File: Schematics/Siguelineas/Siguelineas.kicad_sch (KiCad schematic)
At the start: 25 parts, among them J1 Batt_Input, J11 SD_con, J2 FAN_IN, J3 Line_Sensors, J3 TB6612FNG_A, J4 IMU, J4 TB6612FNG_B, J5 SCREEN, J8 Motor_1, J9 Motor_2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

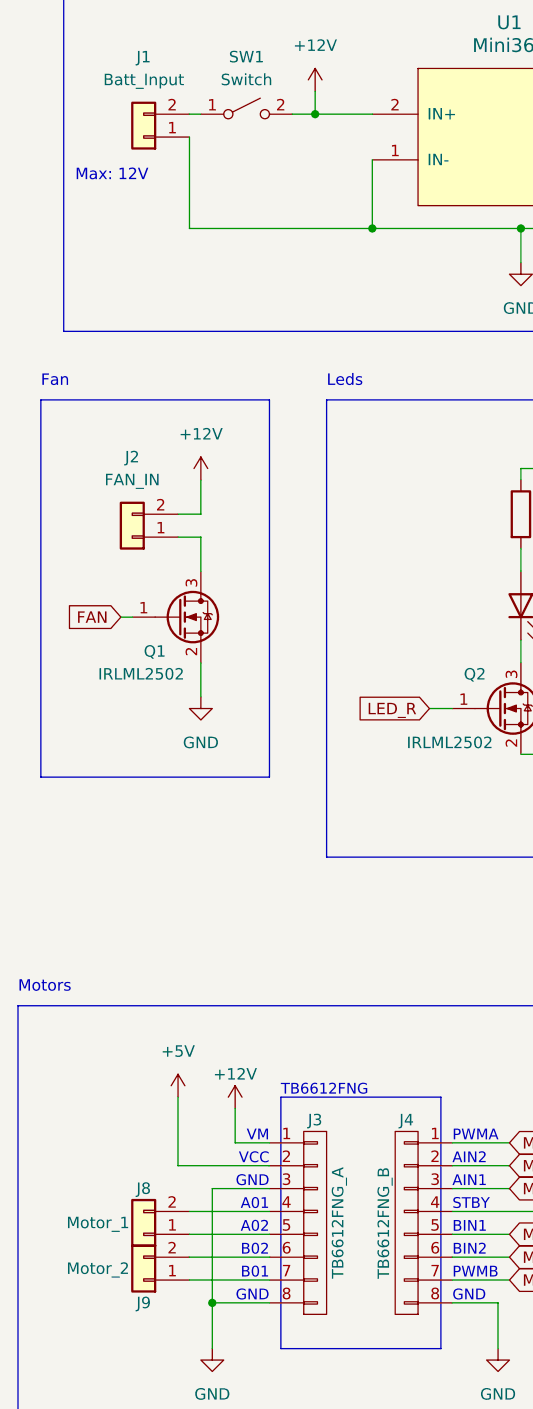
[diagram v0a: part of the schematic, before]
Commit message: Changed motor conectors position
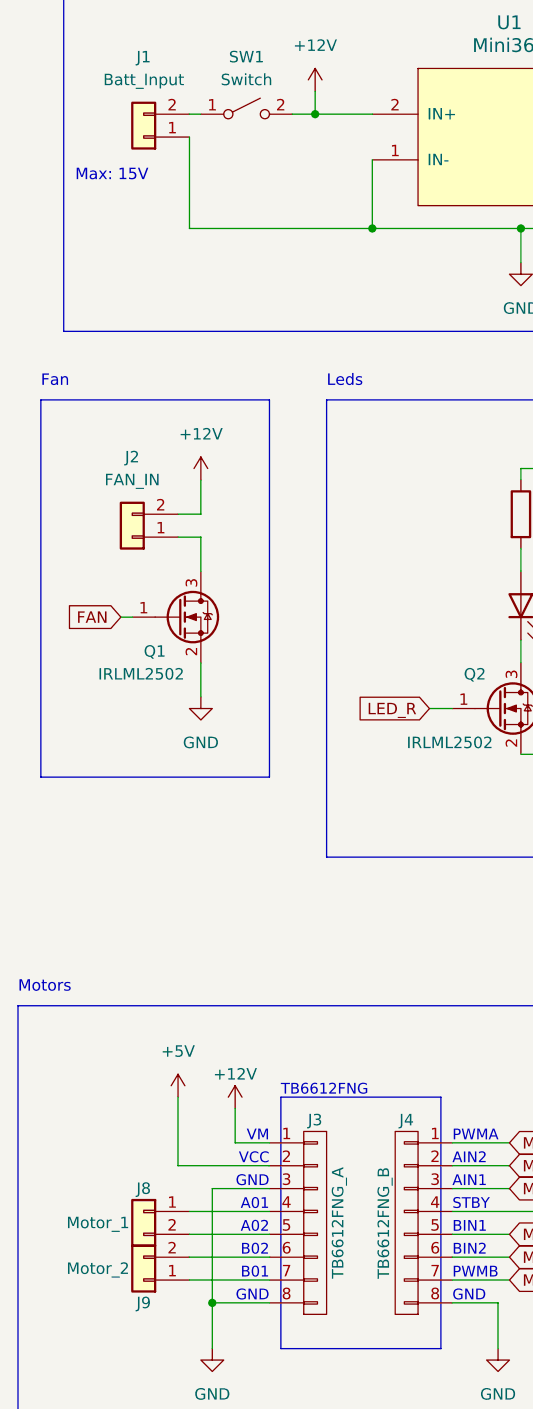
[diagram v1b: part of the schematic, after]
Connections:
- net at J3.4 (P4): now also J8.1 (Pin_1); no longer J8.2 (Pin_2)
- net at J3.5 (P5): now also J8.2 (Pin_2); no longer J8.1 (Pin_1)
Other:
- note added: "Max: 15V"
- note removed: "Max: 12V"
- moved on the sheet: J8
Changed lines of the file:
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@@
+    (stroke (width 0) (type default))
+  )
+  (wire (pts (xy 40.64 161.29) (xy 49.53 161.29))
     (stroke (width 0) (type default))
   )
@@
     (stroke (width 0) (type default))
   )
+  (wire (pts (xy 40.64 158.75) (xy 49.53 158.75))
+    (stroke (width 0) (type default))
+  )
   (wire (pts (xy 175.26 93.98) (xy 177.8 93.98))
     (stroke (width 0) (type default))
@@
     (stroke (width 0) (type default))
   )
-  (wire (pts (xy 40.64 158.75) (xy 49.53 158.75))
-    (stroke (width 0) (type default))
-  )
   (wire (pts (xy 76.2 151.13) (xy 69.85 151.13))
     (stroke (width 0) (type default))
@@
   )
   (wire (pts (xy 175.26 66.04) (xy 177.8 66.04))
-    (stroke (width 0) (type default))
-  )
-  (wire (pts (xy 40.64 161.29) (xy 49.53 161.29))
     (stroke (width 0) (type default))
   )
@@
     (effects (font (size 1.1938 1.1938)) (justify right bottom))
   )
-  (text "Max: 12V" (at 27.94 44.45 0)
+  (text "Max: 15V" (at 27.94 44.45 0)
     (effects (font (size 1.27 1.27)) (justify left bottom))
   )
@@
     )
   )
-  (symbol (lib_id "Connector_Generic:Conn_01x02") (at 35.56 161.29 180) (unit 1)
+  (symbol (lib_id "Connector_Generic:Conn_01x02") (at 35.56 158.75 0) (mirror y) (unit 1)
     (in_bom yes) (on_board yes) (dnp no)
     (property "Reference" "J8" (at 35.56 156.21 0)
@@
       (effects (font (size 1.27 1.27)))
     )
-    (property "Footprint" "Connector_JST:JST_PH_B2B-PH-K_1x02_P2.00mm_Vertical" (at 35.56 161.29 0)
-      (effects (font (size 1.27 1.27)) hide)
-    )
-    (property "Datasheet" "~" (at 35.56 161.29 0)
-      (effects (font (size 1.27 1.27)) hide)
-    )
+    (property "Footprint" "Connector_JST:JST_PH_B2B-PH-K_1x02_P2.00mm_Vertical" (at 35.56 158.75 0)
+      (effects (font (size 1.27 1.27)) hide)
+    )
+    (property "Datasheet" "~" (at 35.56 158.75 0)
+      (effects (font (size 1.27 1.27)) hide)
+    )

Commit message: Version 1.0
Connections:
- net +12V: now also J1.2 (Pin_2); no longer SW1.2 (B)
- net +5V: now also SW1.2 (B); no longer U1.4 (OUT+)
- net at SW1.1 (A): now also U1.4 (OUT+); no longer J1.2 (Pin_2)
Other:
- moved on the sheet: SW1, U1
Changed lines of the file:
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@@
     (comment 1 "Adrian Martinez")
   )
+  (junction (at 44.45 36.83) (diameter 0) (color 0 0 0 0)
+  )
   (junction (at 82.55 107.95) (diameter 0) (color 0 0 0 0)
   )
-  (junction (at 54.61 36.83) (diameter 0) (color 0 0 0 0)
-  )
   (junction (at 256.54 138.43) (diameter 0) (color 0 0 0 0)
   )
@@
   (junction (at 143.51 139.7) (diameter 0) (color 0 0 0 0)
   )
-  (junction (at 60.96 49.53) (diameter 0) (color 0 0 0 0)
+  (junction (at 63.5 49.53) (diameter 0) (color 0 0 0 0)
   )
   (junction (at 259.08 125.73) (diameter 0) (color 0 0 0 0)
@@
   (junction (at 256.54 148.59) (diameter 0) (color 0 0 0 0)
   )
-  (junction (at 77.47 49.53) (diameter 0) (color 0 0 0 0)
-  )
   (junction (at 256.54 140.97) (diameter 0) (color 0 0 0 0)
   )
   (junction (at 43.18 168.91) (diameter 0) (color 0 0 0 0)
+  )
+  (junction (at 48.26 49.53) (diameter 0) (color 0 0 0 0)
   )
   (junction (at 143.51 163.83) (diameter 0) (color 0 0 0 0)
@@
   (no_connect (at 262.89 143.51))
   (no_connect (at 262.89 146.05))
-  (wire (pts (xy 52.07 36.83) (xy 54.61 36.83))
-    (stroke (width 0) (type default))
-  )
   (wire (pts (xy 40.64 161.29) (xy 49.53 161.29))
     (stroke (width 0) (type default))
@@
     (stroke (width 0) (type default))
   )
+  (wire (pts (xy 63.5 49.53) (xy 78.74 49.53))
+    (stroke (width 0) (type default))
+  )
   (wire (pts (xy 40.64 158.75) (xy 49.53 158.75))
     (stroke (width 0) (type default))
@@
     (stroke (width 0) (type default))
   )
-  (wire (pts (xy 54.61 36.83) (xy 54.61 34.29))
+  (wire (pts (xy 44.45 36.83) (xy 44.45 34.29))
     (stroke (width 0) (type default))
   )
@@
     (stroke (width 0) (type default))
   )
+  (wire (pts (xy 44.45 36.83) (xy 48.26 36.83))
+    (stroke (width 0) (type default))
+  )
   (wire (pts (xy 87.63 95.25) (xy 87.63 97.79))
     (stroke (width 0) (type default))
@@
     (stroke (width 0) (type default))
   )
-  (wire (pts (xy 60.96 41.91) (xy 60.96 49.53))
+  (wire (pts (xy 48.26 41.91) (xy 48.26 49.53))
     (stroke (width 0) (type default))
   )
@@
     (stroke (width 0) (type default))
   )
+  (wire (pts (xy 91.44 36.83) (xy 95.25 36.83))
+    (stroke (width 0) (type default))
+  )
   (wire (pts (xy 256.54 138.43) (xy 262.89 138.43))
     (stroke (width 0) (type default))
@@
     (stroke (width 0) (type default))
   )
+  (wire (pts (xy 48.26 49.53) (xy 63.5 49.53))
+    (stroke (width 0) (type default))
+  )
   (wire (pts (xy 237.49 39.37) (xy 228.6 39.37))
     (stroke (width 0) (type default))
@@
     (stroke (width 0) (type default))
   )
-  (wire (pts (xy 91.44 36.83) (xy 95.25 36.83))
-    (stroke (width 0) (type default))
-  )
   (wire (pts (xy 39.37 83.82) (xy 41.91 83.82))
     (stroke (width 0) (type default))
@@
     (stroke (width 0) (type default))
   )
+  (wire (pts (xy 78.74 36.83) (xy 81.28 36.83))
+    (stroke (width 0) (type default))
+  )
   (wire (pts (xy 41.91 77.47) (xy 41.91 81.28))
     (stroke (width 0) (type default))
@@
     (stroke (width 0) (type default))
   )
-  (wire (pts (xy 77.47 49.53) (xy 77.47 53.34))
+  (wire (pts (xy 63.5 49.53) (xy 63.5 52.07))
     (stroke (width 0) (type default))
   )
@@
     (stroke (width 0) (type default))
   )
-  (wire (pts (xy 54.61 36.83) (xy 60.96 36.83))
-    (stroke (width 0) (type default))
-  )
-  (wire (pts (xy 40.64 49.53) (xy 60.96 49.53))
+  (wire (pts (xy 40.64 49.53) (xy 48.26 49.53))
     (stroke (width 0) (type default))
   )
@@
     (stroke (width 0) (type default))
   )
-  (wire (pts (xy 40.64 36.83) (xy 41.91 36.83))
-    (stroke (width 0) (type default))
-  )
   (wire (pts (xy 76.2 153.67) (xy 69.85 153.67))
     (stroke (width 0) (type default))
@@
     (stroke (width 0) (type default))
   )
-  (wire (pts (xy 60.96 49.53) (xy 77.47 49.53))
-    (stroke (width 0) (type default))
-  )
   (wire (pts (xy 175.26 101.6) (xy 176.53 101.6))
     (stroke (width 0) (type default))
@@
     (stroke (width 0) (type default))
   )
-  (wire (pts (xy 91.44 49.53) (xy 77.47 49.53))
-    (stroke (width 0) (type default))
-  )
   (wire (pts (xy 49.53 166.37) (xy 40.64 166.37))
     (stroke (width 0) (type default))
   )
+  (wire (pts (xy 40.64 36.83) (xy 44.45 36.83))
+    (stroke (width 0) (type default))
+  )
   (wire (pts (xy 82.55 76.2) (xy 87.63 76.2))
     (stroke (width 0) (type default))
@@
     (stroke (width 0) (type default))
   )
-  (wire (pts (xy 91.44 41.91) (xy 91.44 49.53))
+  (wire (pts (xy 78.74 41.91) (xy 78.74 49.53))
     (stroke (width 0) (type default))
   )
@@
     )
   )
-  (symbol (lib_id "Switch:SW_SPST") (at 46.99 36.83 0) (unit 1)
-    (in_bom yes) (on_board yes) (dnp no) (fields_autoplaced)
-    (property "Reference" "SW1" (at 46.99 30.48 0)
-      (effects (font (size 1.27 1.27)))
-    )
-    (property "Value" "Switch" (at 46.99 33.02 0)
-      (effects (font (size 1.27 1.27)))
-    )
-    (property "Footprint" "Button_Switch_THT:SW_CuK_OS102011MA1QN1_SPDT_Angled" (at 46.99 36.83 0)
-      (effects (font (size 1.27 1.27)) hide)
-    )
-    (property "Datasheet" "~" (at 46.99 36.83 0)
+  (symbol (lib_id "Switch:SW_SPST") (at 86.36 36.83 0) (unit 1)
+    (in_bom yes) (on_board yes) (dnp no) (fields_autoplaced)
+    (property "Reference" "SW1" (at 86.36 30.48 0)
+      (effects (font (size 1.27 1.27)))
+    )
+    (property "Value" "Switch" (at 86.36 33.02 0)
+      (effects (font (size 1.27 1.27)))
+    )
+    (property "Footprint" "Button_Switch_THT:SW_CuK_OS102011MA1QN1_SPDT_Angled" (at 86.36 36.83 0)
+      (effects (font (size 1.27 1.27)) hide)
+    )
+    (property "Datasheet" "~" (at 86.36 36.83 0)
       (effects (font (size 1.27 1.27)) hide)
     )
@@
     )
   )
-  (symbol (lib_id "power:+12V") (at 54.61 34.29 0) (unit 1)
-    (in_bom yes) (on_board yes) (dnp no) (fields_autoplaced)
-    (property "Reference" "#PWR01" (at 54.61 38.1 0)
-      (effects (font (size 1.27 1.27)) hide)
-    )
-    (property "Value" "+12V" (at 54.61 29.21 0)
-      (effects (font (size 1.27 1.27)))
-    )
-    (property "Footprint" "" (at 54.61 34.29 0)
-      (effects (font (size 1.27 1.27)) hide)
-    )
-    (property "Datasheet" "" (at 54.61 34.29 0)
+  (symbol (lib_id "power:+12V") (at 44.45 34.29 0) (unit 1)
+    (in_bom yes) (on_board yes) (dnp no) (fields_autoplaced)
+    (property "Reference" "#PWR01" (at 44.45 38.1 0)
+      (effects (font (size 1.27 1.27)) hide)
+    )
+    (property "Value" "+12V" (at 44.45 29.21 0)
+      (effects (font (size 1.27 1.27)))
+    )
+    (property "Footprint" "" (at 44.45 34.29 0)
+      (effects (font (size 1.27 1.27)) hide)
+    )
+    (property "Datasheet" "" (at 44.45 34.29 0)
       (effects (font (size 1.27 1.27)) hide)
     )
@@
     )
   )
-  (symbol (lib_id "power:GND") (at 77.47 53.34 0) (unit 1)
+  (symbol (lib_id "power:GND") (at 63.5 52.07 0) (unit 1)
     (in_bom yes) (on_board yes) (dnp no)
-    (property "Reference" "#PWR02" (at 77.47 59.69 0)
-      (effects (font (size 1.27 1.27)) hide)
-    )
-    (property "Value" "GND" (at 77.47 58.42 0)
-      (effects (font (size 1.27 1.27)))
-    )
-    (property "Footprint" "" (at 77.47 53.34 0)
-      (effects (font (size 1.27 1.27)) hide)
-    )
-    (property "Datasheet" "" (at 77.47 53.34 0)
+    (property "Reference" "#PWR02" (at 63.5 58.42 0)
+      (effects (font (size 1.27 1.27)) hide)
+    )
+    (property "Value" "GND" (at 63.5 57.15 0)
+      (effects (font (size 1.27 1.27)))
+    )
+    (property "Footprint" "" (at 63.5 52.07 0)
+      (effects (font (size 1.27 1.27)) hide)
+    )
+    (property "Datasheet" "" (at 63.5 52.07 0)
       (effects (font (size 1.27 1.27)) hide)
     )
@@
     )
   )
-  (symbol (lib_id "mini360:Mini360") (at 76.2 39.37 0) (unit 1)
-    (in_bom yes) (on_board yes) (dnp no) (fields_autoplaced)
-    (property "Reference" "U1" (at 76.2 26.67 0)
+  (symbol (lib_id "mini360:Mini360") (at 63.5 39.37 0) (unit 1)
+    (in_bom yes) (on_board yes) (dnp no) (fields_autoplaced)
+    (property "Reference" "U1" (at 63.5 26.67 0)
       (effects (font (size 1.524 1.524)))
     )
-    (property "Value" "Mini360" (at 76.2 29.21 0)
+    (property "Value" "Mini360" (at 63.5 29.21 0)
       (effects (font (size 1.524 1.524)))
     )
-    (property "Footprint" "Mini360_step-down:Mini360_step-down" (at 76.2 39.37 0)
+    (property "Footprint" "Mini360_step-down:Mini360_step-down" (at 63.5 39.37 0)
       (effects (font (size 1.524 1.524)) hide)
     )
-    (property "Datasheet" "" (at 76.2 39.37 0)
+    (property "Datasheet" "" (at 63.5 39.37 0)
       (effects (font (size 1.524 1.524)) hide)
     )

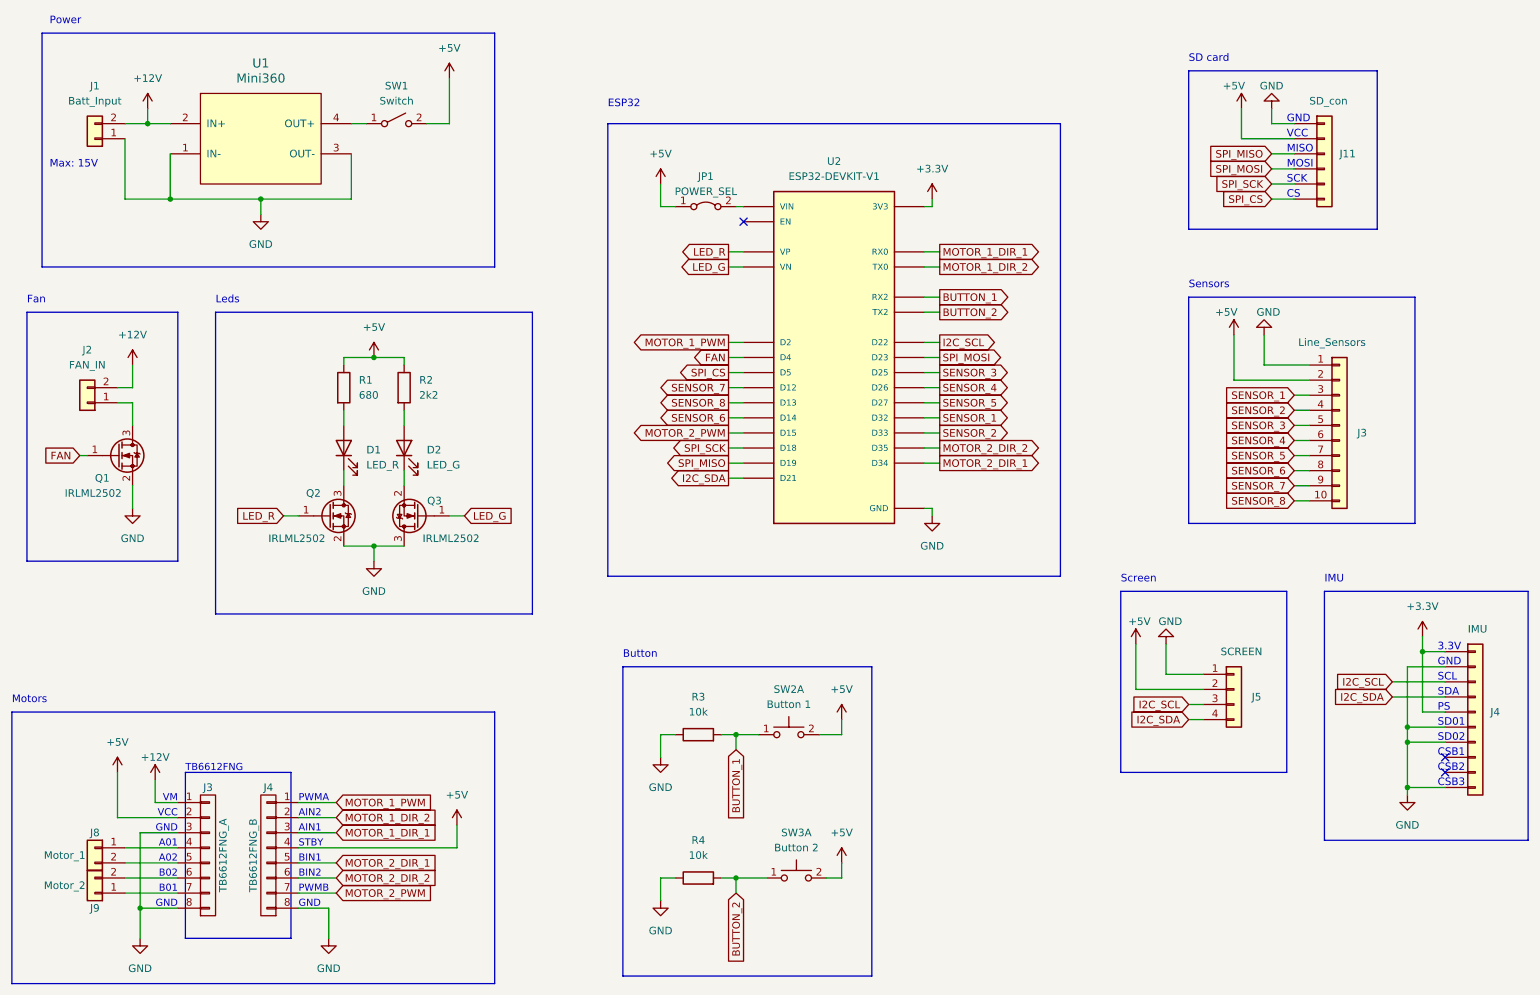
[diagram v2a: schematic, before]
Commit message: Big clean to remove unused componentes, board reworked, v1.1
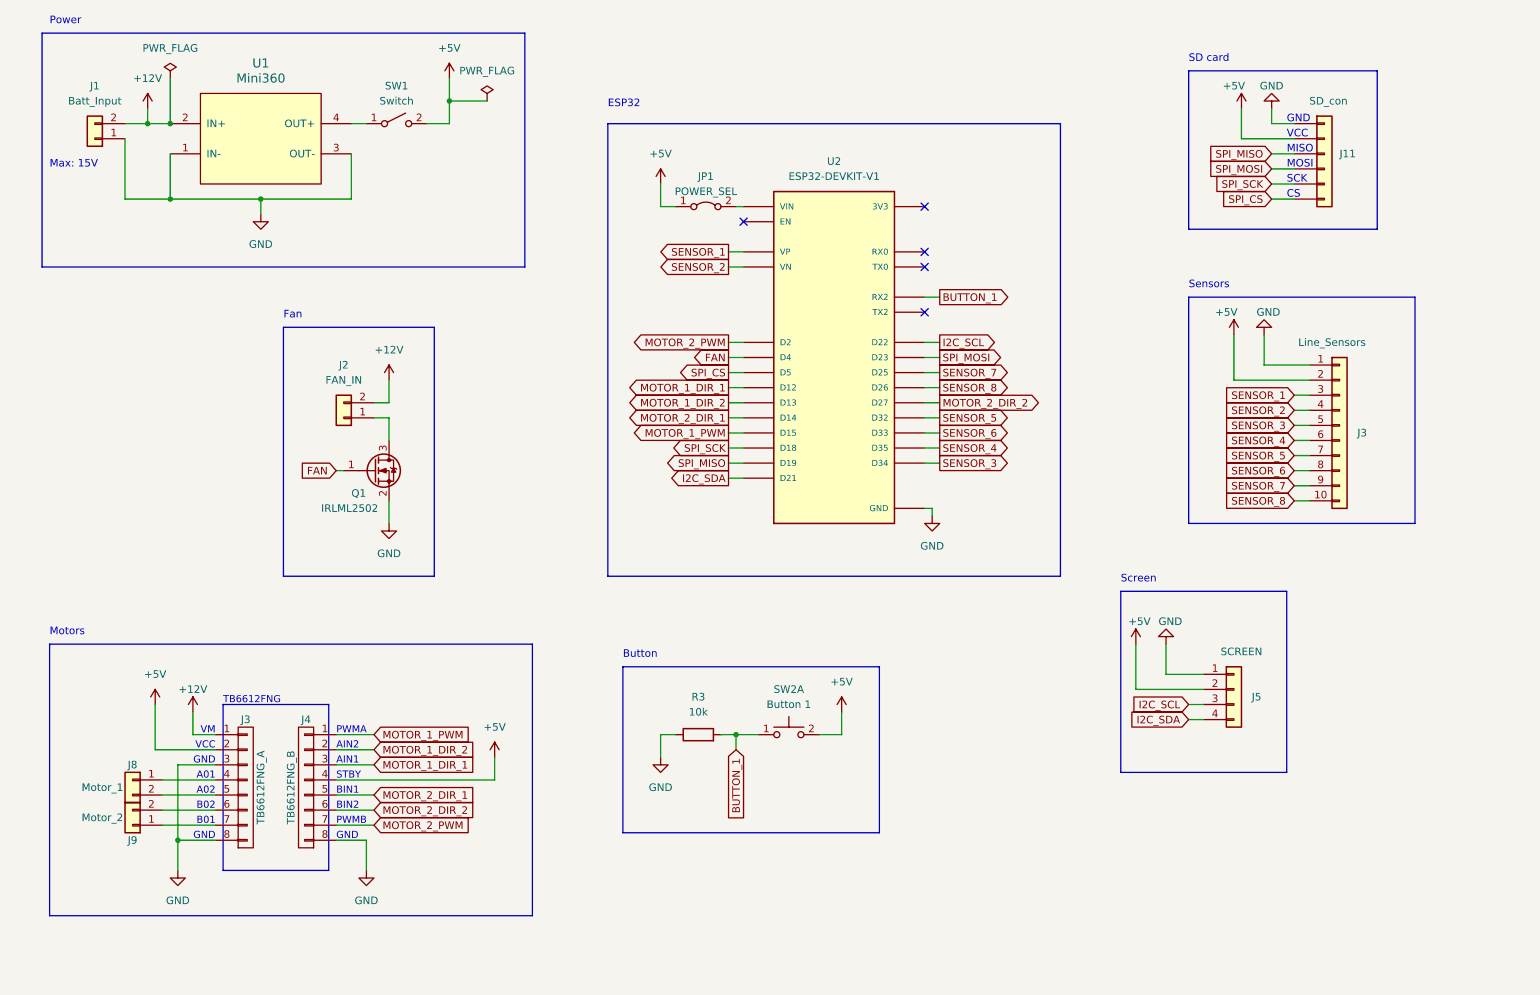
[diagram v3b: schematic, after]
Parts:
- removed D1: LED_R, Diode_SMD:D_1206_3216Metric_Pad1.42x1.75mm_HandSolder, symbol Device:LED
- removed D2: LED_G, Diode_SMD:D_1206_3216Metric_Pad1.42x1.75mm_HandSolder, symbol Device:LED
- removed J4: IMU, Connector_PinSocket_2.54mm:PinSocket_1x10_P2.54mm_Vertical, symbol Connector_Generic:Conn_01x10
- removed Q2, Q3: IRLML2502, Package_TO_SOT_SMD:SOT-23, symbol Device:Q_NMOS_GSD
- removed R1: 680, Resistor_SMD:R_1206_3216Metric_Pad1.30x1.75mm_HandSolder, symbol Device:R
- removed R2: 2k2, Resistor_SMD:R_1206_3216Metric_Pad1.30x1.75mm_HandSolder, symbol Device:R
- removed R4: 10k, Resistor_SMD:R_1206_3216Metric_Pad1.30x1.75mm_HandSolder, symbol Device:R
- removed SW3: Button 2, Button_Switch_THT:SW_PUSH_6mm, symbol Switch:SW_Push_Dual_x2
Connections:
- net LED_G is gone; now on net SENSOR_2: U2.18 (VN)
- net LED_R is gone; now on net SENSOR_1: U2.17 (VP)
- net MOTOR_1_DIR_1: now also U2.27 (D12); no longer U2.12 (RX0)
- net MOTOR_1_DIR_2: now also U2.28 (D13); no longer U2.13 (TX0)
- net MOTOR_1_PWM: now also U2.3 (D15); no longer U2.4 (D2)
- net MOTOR_2_DIR_1: now also U2.26 (D14); no longer U2.19 (D34)
- net MOTOR_2_DIR_2: now also U2.25 (D27); no longer U2.20 (D35)
- net MOTOR_2_PWM: now also U2.4 (D2); no longer U2.3 (D15)
- net SENSOR_1: no longer U2.21 (D32)
- net SENSOR_2: no longer U2.22 (D33)
- net SENSOR_3: now also U2.19 (D34); no longer U2.23 (D25)
- net SENSOR_4: now also U2.20 (D35); no longer U2.24 (D26)
- net SENSOR_5: now also U2.21 (D32); no longer U2.25 (D27)
- net SENSOR_6: now also U2.22 (D33); no longer U2.26 (D14)
- net SENSOR_7: now also U2.23 (D25); no longer U2.27 (D12)
- net SENSOR_8: now also U2.24 (D26); no longer U2.28 (D13)
- net +3.3V: no longer names the net of U2.1 (3V3)
- net BUTTON_2: no longer names the net of U2.7 (TX2)
- no-connect marks 3 -> 5
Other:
- note removed: "3.3V"
- note removed: "CSB1"
- note removed: "CSB2"
- note removed: "CSB3"
- note removed: "IMU"
- note removed: "Leds"
- note removed: "PS"
- note removed: "SCL"
- note removed: "SD01"
- note removed: "SD02"
- note removed: "SDA"
- moved on the sheet: J2, J3, J4, J8, J9, Q1
